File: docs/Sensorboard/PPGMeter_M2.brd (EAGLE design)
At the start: 73.3 x 63.5 mm, 37 parts, among them Q1 SI2302, Q2 SI2302, Q3 SI2302, T1 MAX6675, T2 MAX6675, T3P BMP280

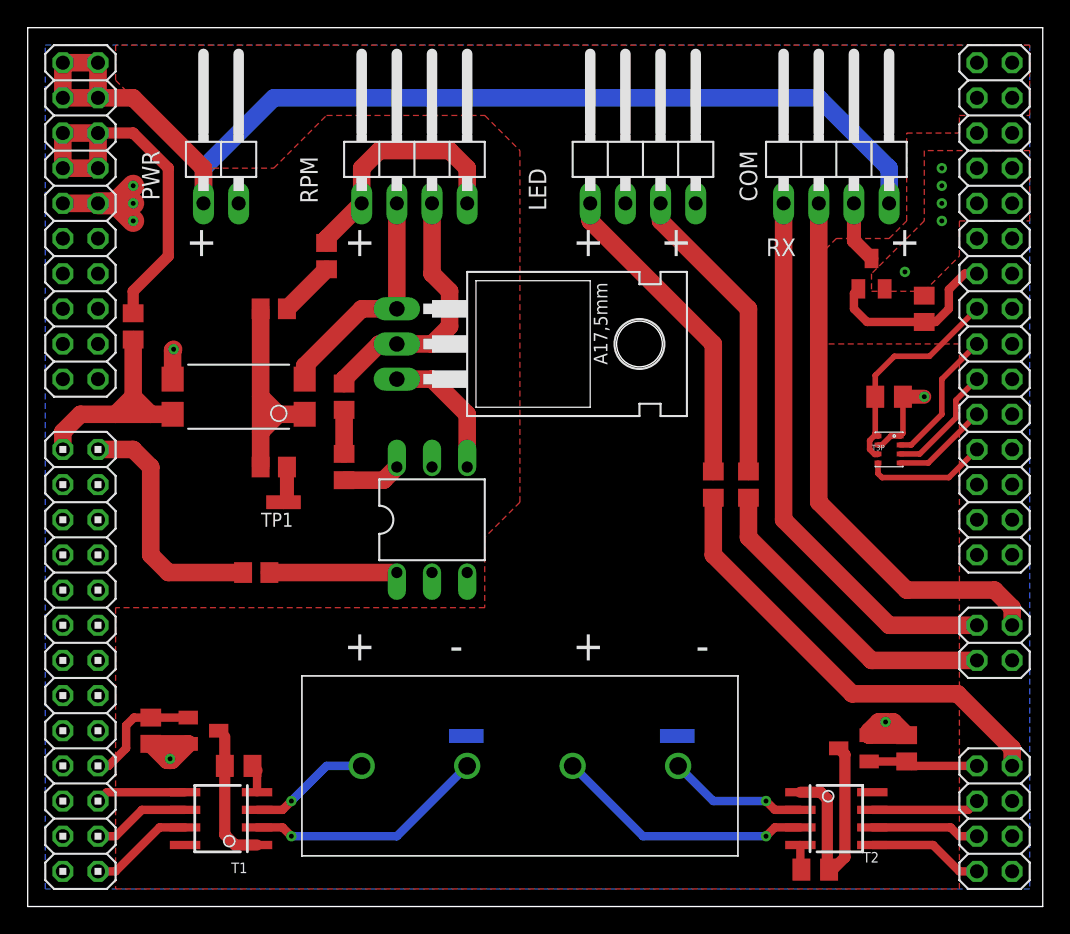
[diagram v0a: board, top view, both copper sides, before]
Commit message: Fixed buffer reading in App.
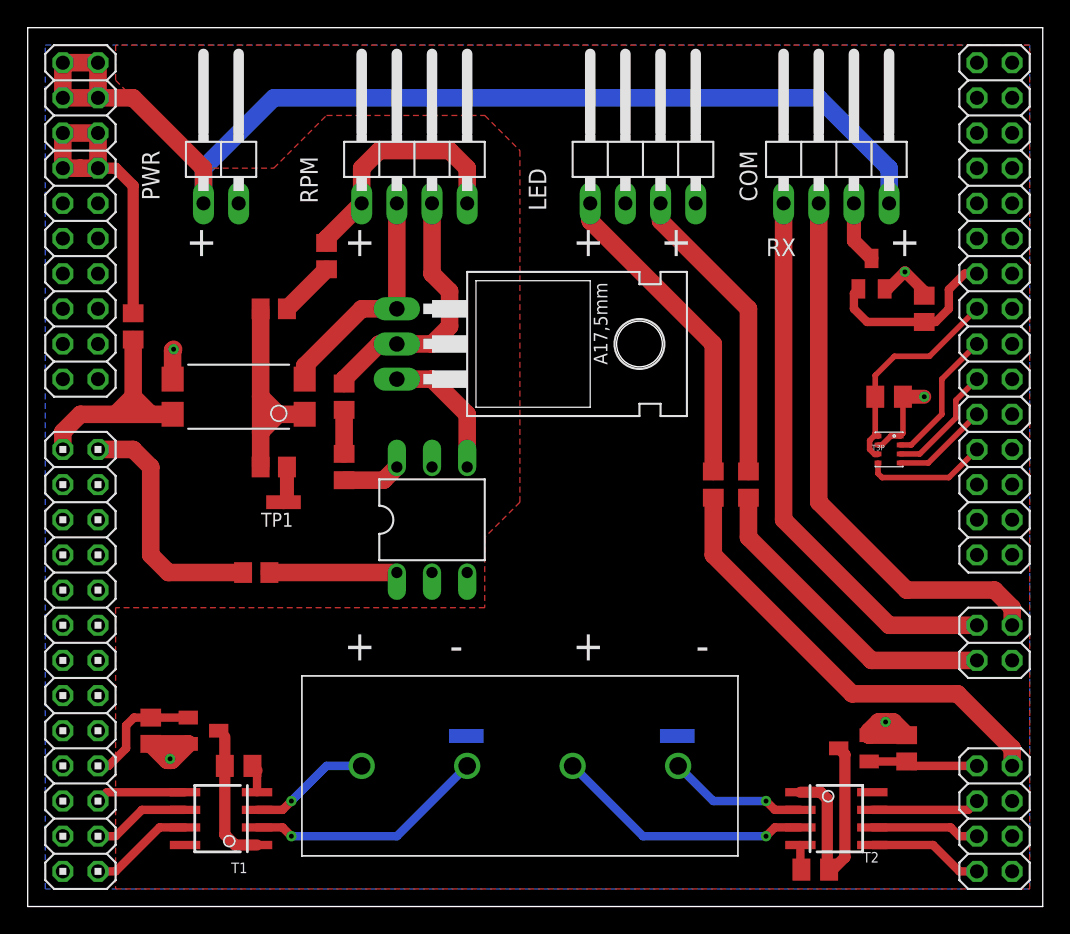
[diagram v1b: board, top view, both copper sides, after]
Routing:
- net GND: track 30.1 -> 25.7 mm, vias 12 -> 5
- net VDD3.3: track 27.8 -> 23.7 mm
- removed copper zone on layer 1, net GND
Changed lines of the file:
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@@
 <vertex x="17.78" y="27.94"/>
 <vertex x="17.78" y="7.62"/>
-<vertex x="78.74" y="7.62"/>
-<vertex x="78.74" y="46.99"/>
-<vertex x="68.58" y="46.99"/>
-<vertex x="68.58" y="53.34"/>
-<vertex x="69.85" y="54.61"/>
-<vertex x="73.66" y="54.61"/>
-<vertex x="74.93" y="55.88"/>
-<vertex x="74.93" y="62.23"/>
-<vertex x="78.74" y="62.23"/>
-<vertex x="78.74" y="63.5"/>
-<vertex x="83.82" y="63.5"/>
+<vertex x="83.82" y="7.62"/>
 <vertex x="83.82" y="68.58"/>
 </polygon>
@@
 <wire x1="16.51" y1="62.23" x2="13.97" y2="62.23" width="1.27" layer="1"/>
 <wire x1="13.97" y1="62.23" x2="13.97" y2="59.69" width="1.27" layer="1"/>
-<wire x1="13.97" y1="59.69" x2="16.51" y2="59.69" width="1.27" layer="1"/>
+<wire x1="13.97" y1="59.69" x2="15.24" y2="59.69" width="1.27" layer="1"/>
+<wire x1="15.24" y1="59.69" x2="16.51" y2="59.69" width="1.27" layer="1"/>
 <wire x1="16.51" y1="59.69" x2="16.51" y2="62.23" width="1.27" layer="1"/>
 <contactref element="R10" pad="2"/>
-<wire x1="19.05" y1="62.23" x2="21.59" y2="59.69" width="0.8128" layer="1"/>
-<wire x1="21.59" y1="59.69" x2="21.59" y2="53.34" width="0.8128" layer="1"/>
-<wire x1="21.59" y1="53.34" x2="19.05" y2="50.8" width="0.8128" layer="1"/>
-<wire x1="19.05" y1="50.8" x2="19.05" y2="49.21" width="0.8128" layer="1"/>
-<wire x1="16.51" y1="62.23" x2="19.05" y2="62.23" width="0.8128" layer="1"/>
+<wire x1="19.05" y1="58.42" x2="17.78" y2="59.69" width="0.8128" layer="1"/>
+<wire x1="17.78" y1="59.69" x2="15.24" y2="59.69" width="0.8128" layer="1"/>
+<wire x1="19.05" y1="49.21" x2="19.05" y2="58.42" width="0.8128" layer="1"/>
 </signal>
 <signal name="N$29">
@@
 <vertex x="12.7" y="7.62"/>
 </polygon>
-<via x="77.47" y="58.42" extent="1-16" drill="0.35"/>
 <contactref element="JP3" pad="7"/>
 <contactref element="JP3" pad="8"/>
-<via x="77.47" y="59.69" extent="1-16" drill="0.35"/>
-<via x="77.47" y="57.15" extent="1-16" drill="0.35"/>
 <contactref element="JP3" pad="9"/>
 <contactref element="JP3" pad="10"/>
@@
 <contactref element="JP1" pad="10"/>
 <contactref element="JP1" pad="9"/>
-<wire x1="13.97" y1="57.15" x2="16.51" y2="57.15" width="1.27" layer="1"/>
-<via x="19.05" y="58.42" extent="1-16" drill="0.35"/>
-<via x="19.05" y="55.88" extent="1-16" drill="0.35"/>
-<via x="19.05" y="57.15" extent="1-16" drill="0.35"/>
 <contactref element="Q1" pad="2"/>
 <contactref element="OPTOTRIAC" pad="2"/>
@@
 <via x="76.2" y="43.18" extent="1-16" drill="0.35"/>
 <contactref element="R8" pad="1"/>
-<polygon width="0.254" layer="1" isolate="1.016">
-<vertex x="72.39" y="50.8"/>
-<vertex x="76.2" y="50.8"/>
-<vertex x="78.74" y="53.34"/>
-<vertex x="78.74" y="55.88"/>
-<vertex x="83.82" y="55.88"/>
-<vertex x="83.82" y="60.96"/>
-<vertex x="76.2" y="60.96"/>
-<vertex x="76.2" y="55.88"/>
-<vertex x="72.39" y="52.07"/>
-</polygon>
-<via x="77.47" y="55.88" extent="1-16" drill="0.35"/>
 <wire x1="76.2" y1="43.18" x2="74.66" y2="43.18" width="1.016" layer="1"/>
 <wire x1="74.66" y1="40.545" x2="74.66" y2="43.18" width="0.4064" layer="1"/>
@@
 <wire x1="73.13789375" y1="39.695" x2="73.78789375" y2="40.345" width="0.4064" layer="1"/>
 <wire x1="74.46" y1="40.345" x2="74.66" y2="40.545" width="0.4064" layer="1"/>
-<wire x1="17.78" y1="57.15" x2="19.05" y2="57.15" width="1.6" layer="1"/>
-<wire x1="19.05" y1="58.42" x2="17.78" y2="57.15" width="1.6" layer="1"/>
-<wire x1="17.78" y1="57.15" x2="16.51" y2="57.15" width="1.6" layer="1"/>
-<wire x1="19.05" y1="55.88" x2="17.78" y2="57.15" width="1.6" layer="1"/>
 <contactref element="OPTO" pad="3"/>
 <via x="21.971" y="46.609" extent="1-16" drill="0.35"/>
@@
 <wire x1="74.93" y1="18.73" x2="73.975" y2="19.685" width="1.27" layer="1"/>
 <wire x1="73.975" y1="19.685" x2="73.406" y2="19.685" width="1.27" layer="1"/>
+<wire x1="74.803" y1="52.197" x2="73.576" y2="50.97" width="0.8128" layer="1"/>
+<wire x1="73.576" y1="50.97" x2="73.34" y2="50.97" width="0.8128" layer="1"/>
+<wire x1="74.803" y1="52.197" x2="76.2" y2="50.8" width="0.8128" layer="1"/>
+<wire x1="76.2" y1="50.8" x2="76.2" y2="50.48" width="0.8128" layer="1"/>
 </signal>
 </signals>
